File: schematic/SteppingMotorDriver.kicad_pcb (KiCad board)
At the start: 2 copper layers, 100 x 100 mm, 70 parts, among them J1 5077CR-16SMC2-BK-TR, J2 Barrel_Jack_Switch, J3 Conn_01x02_Pin, J30 MOTOR_CH0, J31 MOTOR_CH1, J32 MOTOR_CH2, J33 MOTOR_CH3, J40 ENC0, J41 ENC1, J42 ENC2, J43 ENC3, J5 Conn_01x04_Pin, J6 Conn_01x04_Pin, J7 Conn_01x04_Pin, J8 Conn_01x04_Pin, SW1 SW_Push, SW2 SW_Push, U1 NCP361SN, U2 ESP32-S3-WROOM-1, U3 MIC5219-3.3YM5, U6 NJM2114, U7 NJM2114

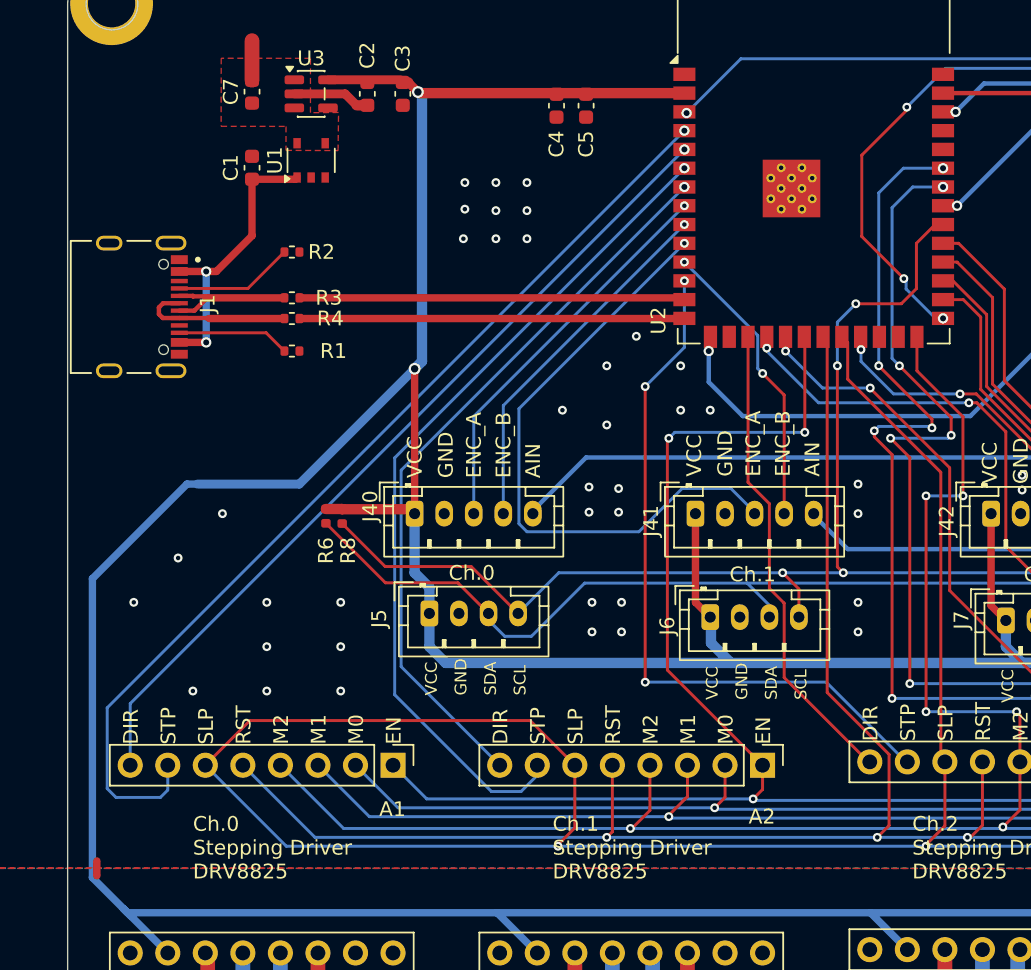
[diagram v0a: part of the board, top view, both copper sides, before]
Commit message: Add firmware skeleton and update schematic: DIP switch removed, MS lines GPIO-driven
- MS0/MS1/MS2 now driven by ESP32-S3 GPIO (GPIO22/23/24) with 100Ω series resistors
- Remove DIP switch from schematic plan and PCB
- Add firmware scaffold: main, motor_ctrl, comm, config modules with sdkconfig
- Add CLAUDE.md project instructions and .gitignore
- Remove stale DRC/session files (SteppingMotorDriver.rules, .ses)

Co-Authored-By: Claude Sonnet 4.6 <noreply@anthropic.com>
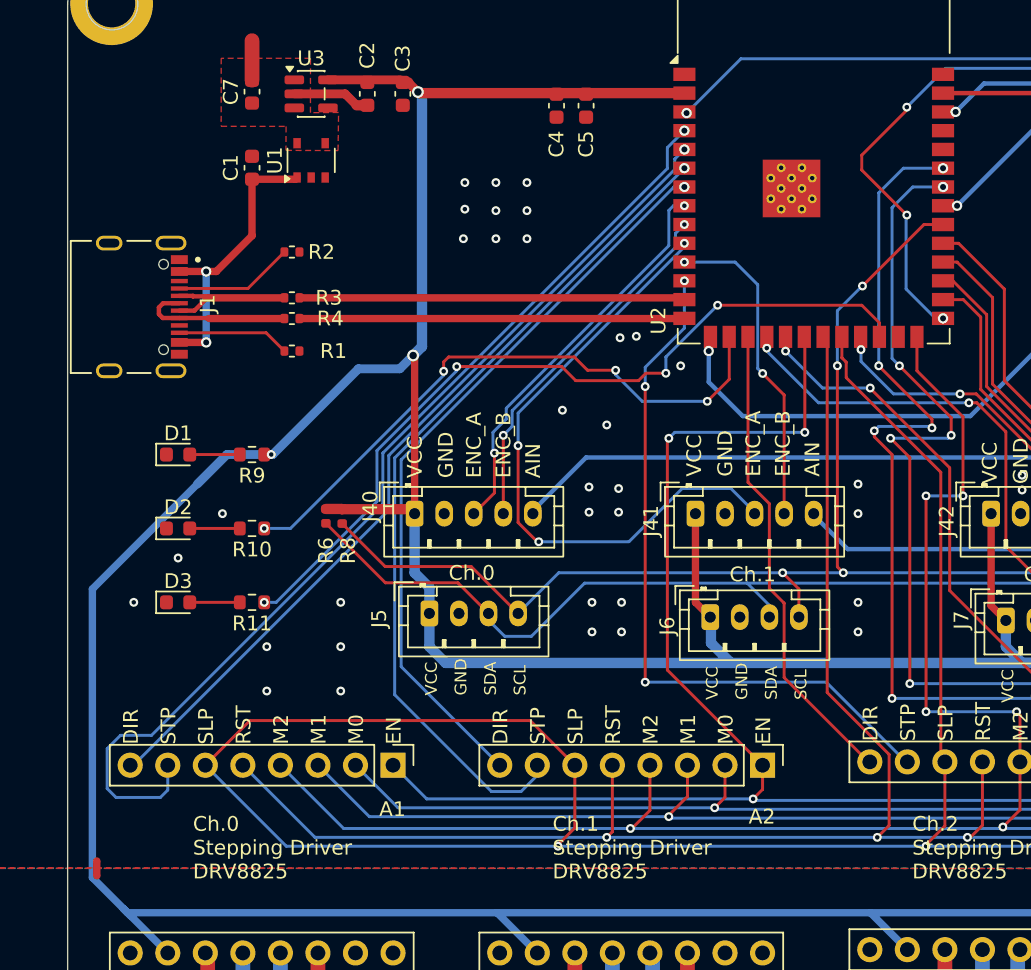
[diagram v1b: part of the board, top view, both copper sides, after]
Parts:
- added D1: LED, LED_SMD:LED_0603_1608Metric, F.Cu at (76.0, 77.0)
- added D2: RED LED, LED_SMD:LED_0603_1608Metric, F.Cu at (76.0, 82.0)
- added D3: YELLOW LED, LED_SMD:LED_0603_1608Metric, F.Cu at (76.0, 87.0)
- added R10: 1k, Resistor_SMD:R_0603_1608Metric, F.Cu at (81.0, 82.0)
- added R11: 1k, Resistor_SMD:R_0603_1608Metric, F.Cu at (81.0, 87.0)
- added R9: 1k, Resistor_SMD:R_0603_1608Metric, F.Cu at (81.0, 77.0)
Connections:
- U2 pad 16: unconnected-(U2-IO46-Pad16) -> /MCU_USB/LED_RED
- U2 pad 24: unconnected-(U2-IO47-Pad24) -> /MCU_USB/LED_YELLOW
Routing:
- net /MCU_USB/LED_YELLOW: track 0.00 -> 55.0 mm, vias 0 -> 4
- net /MCU_USB/LED_RED: track 0.00 -> 41.7 mm, vias 0 -> 4
- net Net-(D3-A): track 0.00 -> 3.39 mm
- net Net-(D2-A): track 0.00 -> 3.39 mm
- net Net-(D1-A): track 0.00 -> 3.39 mm
- net ENC1_B: track 19.8 -> 21.8 mm
- net I2C_SCL: track 113.4 -> 112.1 mm
- net STEP0: track 66.9 -> 68.2 mm
- net ENC1_A: track 41.6 -> 42.2 mm, vias 1 -> 3
- net ENC0_A: track 26.7 -> 27.2 mm, vias 1 -> 2
- net +3V3: track 401.7 -> 402.0 mm, vias 2 -> 3
- net ENC0_B: vias 1 -> 2
- net GND: vias 146 -> 142

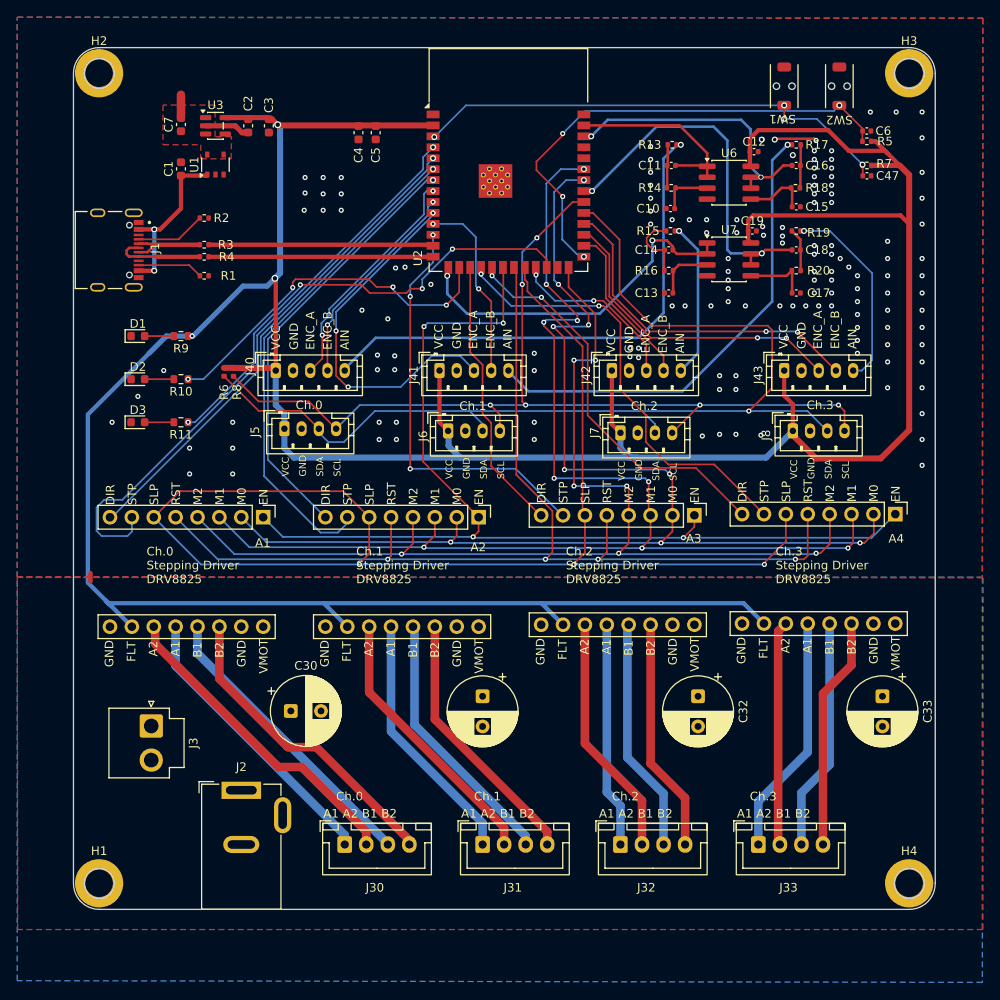
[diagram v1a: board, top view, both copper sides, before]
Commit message: Redesign schematic to 3ch: DRV8825x3, AM26LV32 differential encoder, swap ADC3/ADC4
- DRV8825 stepper driver: 4ch -> 3ch (STEP/DIR CH0-2 on GPIO6-11)
- Encoder: 3ch differential input via AM26LV32IDR for Stepperonline 17HS15-1504-ME1K (1000PPR)
  - A+/A-, B+/B-, Z+/Z- differential pairs, GPIO15-17/18/21/35/36-37/40
- ADC assignment swap: GPIO4=MOT_V(ADC3) voltage monitor, GPIO5=CURRENT(ADC4) 100mOhm+20x amp
- Updated Gerber files (Gerber202960613 replaces Gerber202960504)
- Added AM26LV32IDR and AM26C32INSR library files
- Updated REQUIREMENTS.md: 3ch axis range, encoder specs, ADC channel table, current conversion formula
- Updated CLAUDE.md: corrected GPIO4/5 signal assignments and startup sequence

Co-Authored-By: Claude Sonnet 4.6 <noreply@anthropic.com>
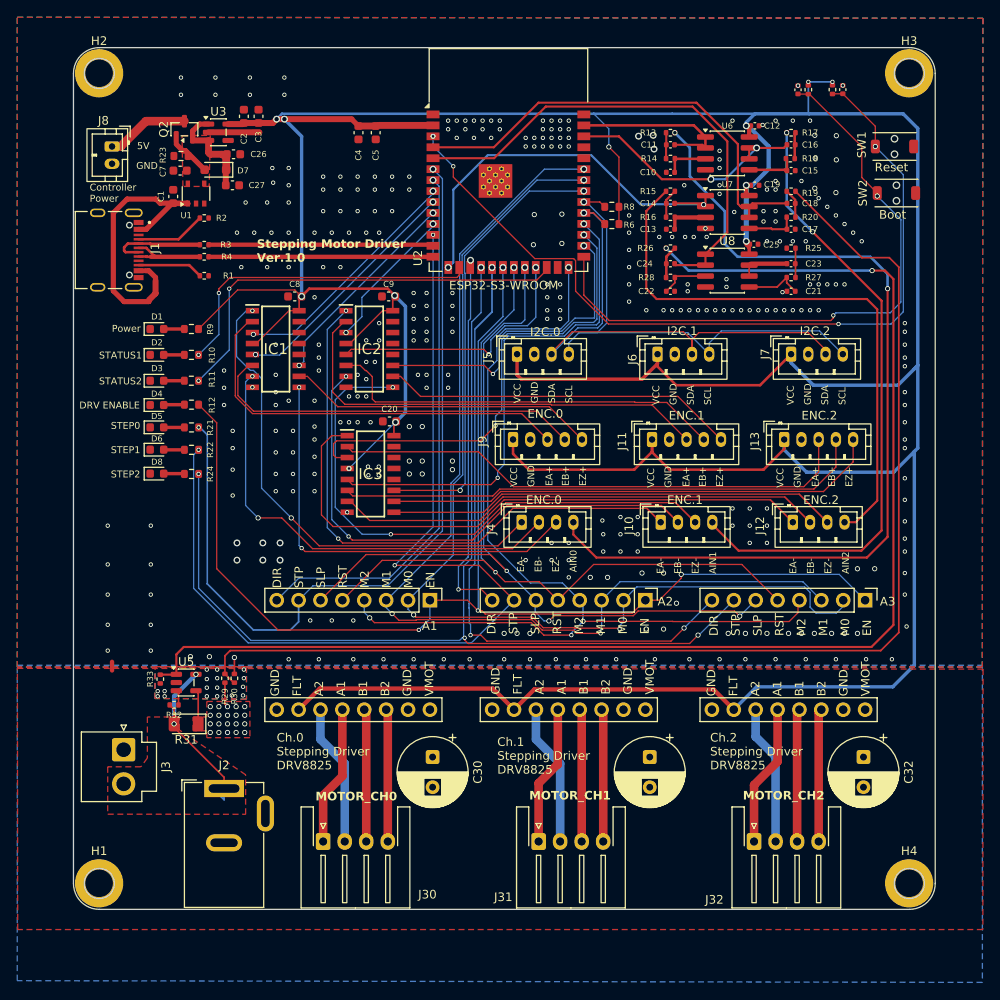
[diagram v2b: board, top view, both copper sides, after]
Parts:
- removed A4: DRV8825_CH3, Library:DRV8825_Driver
- removed C33: 100uF, Capacitor_THT:CP_Radial_D8.0mm_P3.50mm
- removed J33: MOTOR_CH3, Connector_JST:JST_XH_B4B-XH-A_1x04_P2.50mm_Vertical
- removed J40: ENC0, Connector_JST:JST_PH_B5B-PH-K_1x05_P2.00mm_Vertical
- removed J41: ENC1, Connector_JST:JST_PH_B5B-PH-K_1x05_P2.00mm_Vertical
- removed J42: ENC2, Connector_JST:JST_PH_B5B-PH-K_1x05_P2.00mm_Vertical
- removed J43: ENC3, Connector_JST:JST_PH_B5B-PH-K_1x05_P2.00mm_Vertical
- added C20: 0.1uF, Capacitor_SMD:C_0603_1608Metric, F.Cu at (105.2, 86.9)
- added C21: 0.01u, Capacitor_SMD:C_0402_1005Metric, F.Cu at (151.8, 71.8)
- added C22: 0.01u, Capacitor_SMD:C_0402_1005Metric, F.Cu at (137.8, 71.8)
- added C23: 0.01u, Capacitor_SMD:C_0402_1005Metric, F.Cu at (151.8, 68.6)
- added C24: 0.01u, Capacitor_SMD:C_0402_1005Metric, F.Cu at (137.8, 68.6)
- added C25: 0.1uF, Capacitor_SMD:C_0402_1005Metric, F.Cu at (147.5, 66.3)
- added C26: 1uF, Capacitor_SMD:C_0603_1608Metric, F.Cu at (87.1, 55.9)
- added C27: 1uF, Capacitor_SMD:C_0603_1608Metric, F.Cu at (87.0, 59.5)
- added C8: 0.1uF, Capacitor_SMD:C_0603_1608Metric, F.Cu at (94.2, 72.4)
- added C9: 0.1uF, Capacitor_SMD:C_0603_1608Metric, F.Cu at (105.1, 72.4)
- added D4: DRV EN LED, LED_SMD:LED_0603_1608Metric, F.Cu at (78.2, 85.0)
- added D5: STP0 LED, LED_SMD:LED_0603_1608Metric, F.Cu at (78.2, 87.6)
- added D6: STP1 LED, LED_SMD:LED_0603_1608Metric, F.Cu at (78.2, 90.2)
- added D7: CHU20S30, Diode_SMD:D_SOD-323_HandSoldering, F.Cu at (85.0, 57.7)
- added D8: STP2 LED, LED_SMD:LED_0603_1608Metric, F.Cu at (78.2, 93.0)
- added IC1: AM26LV32IDR, Library:SOIC127P600X175-16N, F.Cu at (92.0, 78.5)
- added IC2: AM26LV32IDR, Library:SOIC127P600X175-16N, F.Cu at (102.9, 78.5)
- added IC3: AM26LV32IDR, Library:SOIC127P600X175-16N, F.Cu at (103.0, 93.0)
- added J10: Conn_01x04, Connector_JST:JST_PH_B4B-PH-K_1x04_P2.00mm_Vertical, F.Cu at (136.7, 98.6)
- added J11: Conn_01x05, Connector_JST:JST_PH_B5B-PH-K_1x05_P2.00mm_Vertical, F.Cu at (135.7, 89.0)
- added J12: Conn_01x04, Connector_JST:JST_PH_B4B-PH-K_1x04_P2.00mm_Vertical, F.Cu at (152.0, 98.6)
- added J13: Conn_01x05, Connector_JST:JST_PH_B5B-PH-K_1x05_P2.00mm_Vertical, F.Cu at (151.0, 89.0)
- added J4: Conn_01x04, Connector_JST:JST_PH_B4B-PH-K_1x04_P2.00mm_Vertical, F.Cu at (120.5, 98.6)
- added J9: Conn_01x05, Connector_JST:JST_PH_B5B-PH-K_1x05_P2.00mm_Vertical, F.Cu at (119.5, 89.0)
- added Q2: DMG3415, Package_TO_SOT_SMD:SOT-23, F.Cu at (81.4, 53.0)
- added R12: 1k, Resistor_SMD:R_0603_1608Metric, F.Cu at (82.2, 85.0)
- added R21: 1k, Resistor_SMD:R_0603_1608Metric, F.Cu at (82.2, 87.6)
- added R22: 1k, Resistor_SMD:R_0603_1608Metric, F.Cu at (82.2, 90.2)
- added R23: 100k, Resistor_SMD:R_0603_1608Metric, F.Cu at (81.0, 56.1)
- added R24: 1k, Resistor_SMD:R_0603_1608Metric, F.Cu at (82.2, 93.0)
- added R25: 16k, Resistor_SMD:R_0402_1005Metric, F.Cu at (151.8, 66.8)
- added R26: 16k, Resistor_SMD:R_0402_1005Metric, F.Cu at (137.8, 66.8)
- added R27: 16k, Resistor_SMD:R_0402_1005Metric, F.Cu at (151.8, 70.2)
- added R28: 16k, Resistor_SMD:R_0402_1005Metric, F.Cu at (137.8, 70.2)
- added R29: 68k, Resistor_SMD:R_0402_1005Metric, F.Cu at (86.1, 116.7)
- added R30: 10k, Resistor_SMD:R_0402_1005Metric, F.Cu at (87.2, 116.7)
- added R31: 10m, LED_SMD:LED_1206_3216Metric, F.Cu at (81.6, 122.0)
- added R32: 499, Resistor_SMD:R_0402_1005Metric, F.Cu at (80.2, 119.8)
- added R33: 10k, Resistor_SMD:R_0402_1005Metric, F.Cu at (78.6, 116.8)
- added U5: LT6106, Package_TO_SOT_SMD:SOT-23-5, F.Cu at (81.6, 117.2)
- added U8: NJM8532M, Package_SO:SOP-8_3.76x4.96mm_P1.27mm, F.Cu at (144.4, 69.4)
- J30, J31, J32: footprint Connector_JST:JST_XH_B4B-XH-A_1x04_P2.50mm_Vertical -> Connector_JST:JST_XH_S4B-XH-A-1_1x04_P2.50mm_Horizontal
- J8: value Conn_01x04_Pin -> Conn_01x02; footprint Connector_JST:JST_PH_B4B-PH-K_1x04_P2.00mm_Vertical -> Connector_JST:JST_PH_B2B-PH-K_1x02_P2.00mm_Vertical
- R6, R8: footprint Inductor_SMD:L_0402_1005Metric -> Resistor_SMD:R_0603_1608Metric
- SW1: value SW_Push -> RESET
- U6, U7: value NJM2114 -> NJM8532M
- moved J8 85.6 mm to (73.0, 55.0), turned to -90 degrees
- moved R6 48.2 mm to (131.0, 64.0), turned to 180 degrees
- moved R8 47.9 mm to (131.0, 62.0), turned to 180 degrees
- moved J5 28.4 mm to (120.0, 79.1)
- moved J6 25.9 mm to (136.3, 79.1)
- moved A3 22.1 mm to (160.4, 107.7)
- moved J7 21.8 mm to (151.8, 79.1)
- moved A1 21.6 mm to (109.9, 107.7)
- moved A2 21.6 mm to (134.9, 107.7)
- moved Cr1 20.6 mm to (135.4, 125.8)
- moved C32 20.5 mm to (160.2, 125.8)
- moved C30 17.3 mm to (110.2, 125.8), turned to -90 degrees
- moved J32 15.5 mm to (147.5, 135.7)
- moved SW1 14.6 mm to (163.8, 55.0), turned to 90 degrees
- moved SW2 14.1 mm to (164.0, 60.4), turned to 90 degrees
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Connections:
- J2 pad 1: VIN_24V -> /Power/MOT_POWER_IN
- J3 pad 2: VIN_24V -> /Power/MOT_POWER_IN
- J8 pad 1: +3V3 -> /MCU_USB/5V_IN
- R19 pad 1: AIN3 -> MOV_V
- U2 pad 10: ENC1_A -> ENC0_Z
- U2 pad 11: ENC1_B -> ENC1_A
- U2 pad 12: STEP2 -> STEP1
- U2 pad 17: DIR2 -> DIR1
- U2 pad 18: STEP3 -> STEP2
- U2 pad 19: DIR3 -> DIR2
- U2 pad 23: ENC2_A -> ENC1_B
- U2 pad 28: ENC2_B -> ENC1_Z
- U2 pad 29: ENC3_A -> ENC2_A
- U2 pad 30: ENC3_B -> ENC2_B
- U2 pad 33: ADC3 -> ENC2_Z
- U2 pad 4: STEP0 -> ADC3
- U2 pad 5: DIR0 -> ADC4
- U2 pad 6: STEP1 -> STEP0
- U2 pad 7: DIR1 -> DIR0
- U3 pad 1: /MCU_USB/USB_5V -> Net-(D7-K)
- U3 pad 3: /MCU_USB/USB_5V -> Net-(D7-K)
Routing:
- net CURRENT_V: track 0.00 -> 156.8 mm, vias 0 -> 2
- net MOV_V: track 0.00 -> 140.9 mm
- net +3V3: track 402.0 -> 486.9 mm, vias 3 -> 12
- net STEP2: track 47.9 -> 124.4 mm, vias 3 -> 4
- net /Encoders_IO/ENC_2_EA-: track 0.00 -> 69.1 mm
- net /Encoders_IO/ENC_1_EA-: track 0.00 -> 67.8 mm, vias 0 -> 2
- net /Encoders_IO/ENC_1_EZ-: track 0.00 -> 65.3 mm, vias 0 -> 2
- net /Encoders_IO/ENC_2_EB+: track 0.00 -> 61.6 mm
- net /Encoders_IO/ENC_2_EA+: track 0.00 -> 61.1 mm
- net /Encoders_IO/ENC_1_EB-: track 0.00 -> 60.9 mm, vias 0 -> 2
- net I2C_SDA: track 123.1 -> 62.3 mm
- net /Encoders_IO/ENC_2_EZ+: track 0.00 -> 57.8 mm
- net ADC4: track 0.00 -> 57.4 mm
- net STEP1: track 56.6 -> 113.9 mm, vias 1 -> 3
- net /Encoders_IO/ENC_0_EA-: track 0.00 -> 57.3 mm, vias 0 -> 2
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- added copper zone on F.Cu, net /Power/MOT_POWER_IN
- added copper zone on B.Cu, net GNDPWR
- added copper zone on F.Cu, net VIN_24V
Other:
- board text added: "5V"
- board text added: "AIN0"
- board text added: "AIN1"
- board text added: "AIN2"
- board text added: "Boot"
- board text added: "Controller Power"
- board text added: "DRV ENABLE"
- board text added: "EA+"
- board text added: "EA-"
- board text added: "EB+"
- board text added: "EB-"
- board text added: "ENC.0"
- board text added: "ENC.1"
- board text added: "ENC.2"
- board text added: "ESP32-S3-WROOM"
- board text added: "EZ+"
- board text added: "EZ-"
- board text added: "I2C.0"
- board text added: "I2C.1"
- board text added: "I2C.2"
- board text added: "MOTOR_CH0"
- board text added: "MOTOR_CH1"
- board text added: "MOTOR_CH2"
- board text added: "Power"
- board text added: "Reset"
- board text added: "STATUS1"
- board text added: "STATUS2"
- board text added: "STEP0"
- board text added: "STEP1"
- board text added: "STEP2"
- board text added: "Stepping Motor Driver Ver.1.0"
- board text removed: "AIN"
- board text removed: "Ch.0"
- board text removed: "Ch.1"
- board text removed: "Ch.2"
- board text removed: "Ch.3"
- board text removed: "Ch.3 Stepping Driver DRV8825"
- board text removed: "ENC_A"
- board text removed: "ENC_B"
